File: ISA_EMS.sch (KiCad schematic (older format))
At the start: 91 parts, among them J1 ISA BUS, J10 Parallel Port, J11 Serial 4 IDC, J12 Serial 3 IDC, J13 UART4_SEL, J14 ROM Config, J2 ADDR_IRQ, J3 UART1_SEL, J4 UART2_SEL, J5 ADDR, J6 Serial 2 IDC, J7 Serial 1 DB9, J8 UART3_SEL, J9 Parport IRQ Select, U1 74LS138, U11 74LS30, U12 74LS86, U13 74LS02, U14 74LS155, U15 74LS245, U16 74LS174, U17 74LS374, U18 74LS05, U19 74LS125, U2 74LS138, U20 74LS240, U21 74LS244, U23 16C554, U24 74LS32, U25 GD75232N, U26 GD75232N, U27 SST39SF040, U28 74HCT688, U5 GD75232N, U6 GD75232N, X1 1.8432Mhz

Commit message: Add first ram CHIP
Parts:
- removed C27, C28, C29, C30, C31, C32, C33, C34, C35: 2.2nF, Capacitor_THT:C_Disc_D5.0mm_W2.5mm_P5.00mm, symbol Device:C_Small
- removed D1: LED Channel A, LED_THT:LED_D3.0mm-3, symbol Device:LED_Dual_CAC
- removed D2: LED Channel B, LED_THT:LED_D3.0mm-3, symbol Device:LED_Dual_CAC
- removed D3: LED Channel C, LED_THT:LED_D3.0mm-3, symbol Device:LED_Dual_CAC
- removed D4: LED Channel D, LED_THT:LED_D3.0mm-3, symbol Device:LED_Dual_CAC
- removed J10: Parallel Port, Connector_PinHeader_2.54mm:PinHeader_2x13_P2.54mm_Vertical, symbol Connector_Generic:Conn_02x13_Odd_Even
- removed J11: Serial 4 IDC, Connector_PinHeader_2.54mm:PinHeader_2x05_P2.54mm_Vertical, symbol Connector_Generic:Conn_02x05_Odd_Even
- removed J12: Serial 3 IDC, Connector_PinHeader_2.54mm:PinHeader_2x05_P2.54mm_Vertical, symbol Connector_Generic:Conn_02x05_Odd_Even
- removed J13: UART4_SEL, Connector_PinHeader_2.54mm:PinHeader_1x04_P2.54mm_Vertical, symbol Connector_Generic:Conn_01x04
- removed J2: ADDR_IRQ, Connector_PinHeader_2.54mm:PinHeader_1x08_P2.54mm_Vertical, symbol Connector_Generic:Conn_01x08
- removed J3: UART1_SEL, Connector_PinHeader_2.54mm:PinHeader_1x08_P2.54mm_Vertical, symbol Connector_Generic:Conn_01x08
- removed J4: UART2_SEL, Connector_PinHeader_2.54mm:PinHeader_1x08_P2.54mm_Vertical, symbol Connector_Generic:Conn_01x08
- removed J5: ADDR, Connector_PinHeader_2.54mm:PinHeader_1x04_P2.54mm_Vertical, symbol Connector_Generic:Conn_01x04
- removed J6: Serial 2 IDC, Connector_PinHeader_2.54mm:PinHeader_2x05_P2.54mm_Vertical, symbol Connector_Generic:Conn_02x05_Odd_Even
- removed J7: Serial 1 DB9, Connector_Dsub:DSUB-9_Male_Horizontal_P2.77x2.84mm_EdgePinOffset7.70mm_Housed_MountingHolesOffset9.12mm, symbol Connector:DB9_Male_MountingHoles
- removed J8: UART3_SEL, Connector_PinHeader_2.54mm:PinHeader_1x04_P2.54mm_Vertical, symbol Connector_Generic:Conn_01x04
- removed J9: Parport IRQ Select, Connector_PinHeader_2.54mm:PinHeader_2x04_P2.54mm_Vertical, symbol Connector_Generic:Conn_02x04_Odd_Even
- removed JP1: Address selection, Connector_PinHeader_2.54mm:PinHeader_1x02_P2.54mm_Vertical, symbol Device:Jumper_NO_Small
- removed JP2: Parport type, Connector_PinHeader_2.54mm:PinHeader_1x03_P2.54mm_Vertical, symbol Device:Jumper_NC_Dual
- removed JP3: Interrupt Mode, Connector_PinHeader_2.54mm:PinHeader_1x02_P2.54mm_Vertical, symbol Device:Jumper_NO_Small
- removed R10, R3, R4, R5, R6, R7, R8, R9: 1k, Resistor_THT:R_Axial_DIN0207_L6.3mm_D2.5mm_P10.16mm_Horizontal, symbol Device:R_Small
- removed RN1: 4.7k, Resistor_THT:R_Array_SIP9, symbol Device:R_Network08
- removed RN2: 4.7k, Resistor_THT:R_Array_SIP5, symbol Device:R_Network04
- removed U1, U2: 74LS138, Package_DIP:DIP-16_W7.62mm_LongPads, symbol 74xx:74LS138
- removed U11: 74LS30, Package_DIP:DIP-14_W7.62mm_LongPads, symbol 74xx:74LS30
- removed U12: 74LS86, Package_DIP:DIP-14_W7.62mm_LongPads, symbol 74xx:74LS86
- removed U13: 74LS02, Package_DIP:DIP-14_W7.62mm_LongPads, symbol 74xx:74LS02
- removed U14: 74LS155, Package_DIP:DIP-16_W7.62mm_LongPads, symbol 74xx:74LS155
- removed U15: 74LS245, Package_DIP:DIP-20_W7.62mm_LongPads, symbol 74xx:74LS245
- removed U16: 74LS174, Package_DIP:DIP-16_W7.62mm_LongPads, symbol 74xx:74LS174
- removed U17: 74LS374, Package_DIP:DIP-20_W7.62mm_LongPads, symbol 74xx:74LS374
- removed U18: 74LS05, Package_DIP:DIP-14_W7.62mm_LongPads, symbol 74xx:74LS05
- removed U19: 74LS125, Package_DIP:DIP-14_W7.62mm_LongPads, symbol 74xx:74LS125
- removed U20: 74LS240, Package_DIP:DIP-20_W7.62mm_LongPads, symbol 74xx:74LS240
- removed U21: 74LS244, Package_DIP:DIP-20_W7.62mm_LongPads, symbol 74xx:74LS244
- removed U23: 16C554, Package_LCC:PLCC-68_THT-Socket, symbol custom_components:16554
- removed U24: 74LS32, Package_DIP:DIP-14_W7.62mm_LongPads, symbol 74xx:74LS32
- removed U25, U26, U5, U6: GD75232N, Package_DIP:DIP-20_W7.62mm_LongPads, symbol Interface_UART:GD75232N
- removed X1: 1.8432Mhz, ISA_DualUART:Oscillator_DIP-14-8, symbol Oscillator:CXO_DIP14
- added U3: AS6C4008-55PCN, Package_DIP:DIP-32_W15.24mm, symbol Memory_RAM:AS6C4008-55PCN
- renumbered RN3 to RN1, U28 to U1, U27 to U2
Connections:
- net labels added: DB0, DB1, DB2, DB3, DB4, DB5, DB6, DB7, RAM-A14, RAM-A15, RAM-A16, RAM-A17, RAM-A18, ~RAM-CS0
- net labels removed: 0x2E8, 0x2F8, 0x3E8, 0x3F8, PARPORT_BD0, PARPORT_BD1, PARPORT_BD2, PARPORT_BD3, PARPORT_BD4, PARPORT_BD5, PARPORT_BD6, PARPORT_BD7, PARPORT_BUSY, PARPORT_DATA0, PARPORT_DATA1, PARPORT_DATA2, PARPORT_DATA3, PARPORT_DATA4, PARPORT_DATA5, PARPORT_DATA6, PARPORT_DATA7, PARPORT_DIR, PARPORT_IRQ, PARPORT_IRQEN, PARPORT_PE, PARPORT_R, PARPORT_RPA, PARPORT_RPB, PARPORT_RPC, PARPORT_SLCT, PARPORT_WPA, PARPORT_WPC, RN_1, RN_2, RN_3, RN_4, RN_5, RN_6, RN_7, RN_8, RS232_1_CTS, RS232_1_DCD, RS232_1_DSR, RS232_1_DTR, RS232_1_RI, RS232_1_RTS, RS232_1_RX, RS232_1_TX, RS232_2_CTS, RS232_2_DCD, RS232_2_DSR, RS232_2_DTR, RS232_2_RI, RS232_2_RTS, RS232_2_RX, RS232_2_TX, RS232_3_CTS, RS232_3_DCD, RS232_3_DSR, RS232_3_DTR, RS232_3_RI, RS232_3_RTS, RS232_3_RX, RS232_3_TX, RS232_4_CTS, RS232_4_DCD, RS232_4_DSR, RS232_4_DTR, RS232_4_RI, RS232_4_RTS, RS232_4_RX, RS232_4_TX, RX_A, RX_B, RX_C, RX_D, SER_CLK, TX_A, TX_B, TX_C, TX_D, UART1_IRQ, UART2_IRQ, UARTA_IRQ, UARTB_IRQ, UARTC_IRQ, UARTD_IRQ, ~CTS_A, ~CTS_B, ~CTS_C, ~CTS_D, ~DCD_A, ~DCD_B, ~DCD_C, ~DCD_D, ~DSR_A, ~DSR_B, ~DSR_C, ~DSR_D, ~DTR_A, ~DTR_B, ~DTR_C, ~DTR_D, ~PARPORT_ACK, ~PARPORT_AUTOFD, ~PARPORT_ERROR, ~PARPORT_INIT, ~PARPORT_IRQEN, ~PARPORT_RESET, ~PARPORT_SLCTIN, ~PARPORT_STROBE, ~RI_A, ~RI_B, ~RI_C, ~RI_D, ~RTS_A, ~RTS_B, ~RTS_C, ~RTS_D, ~UART1_CS, ~UART2_CS, ~UART3_CS, ~UART4_CS
- wire segments 950 -> 310
- no-connect marks 37 -> 13
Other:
- note removed: "Open - 0x278/9/A\nClosed - 0x378/9/A"
- note removed: "Parallel Port"
- note removed: "Serial Ports"

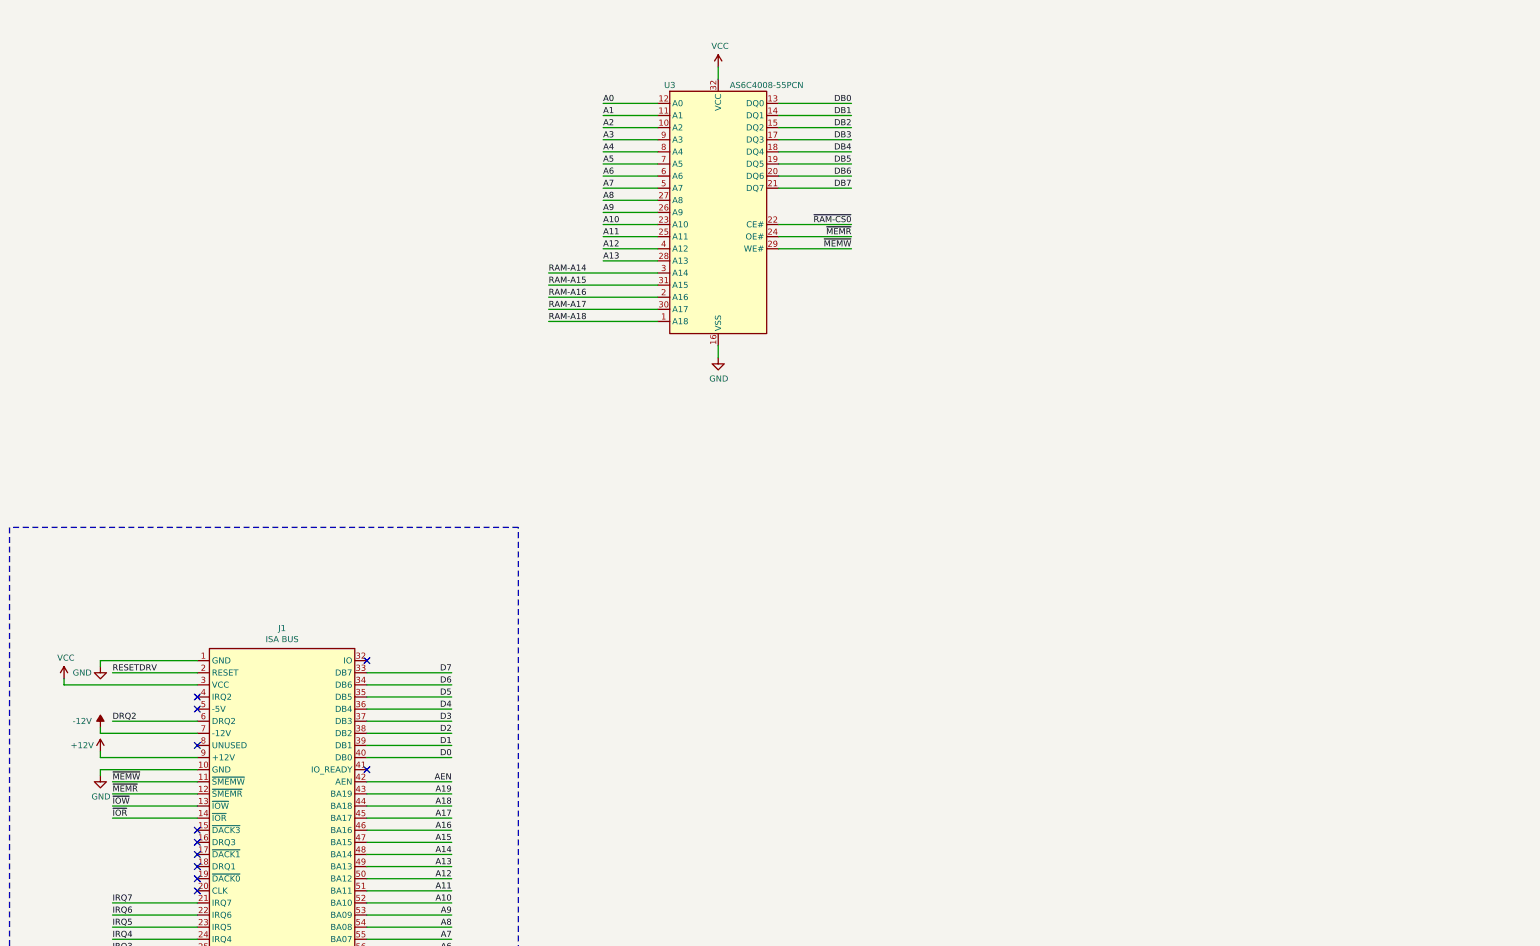
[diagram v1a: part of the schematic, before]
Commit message: Add all the necessary RAM chips
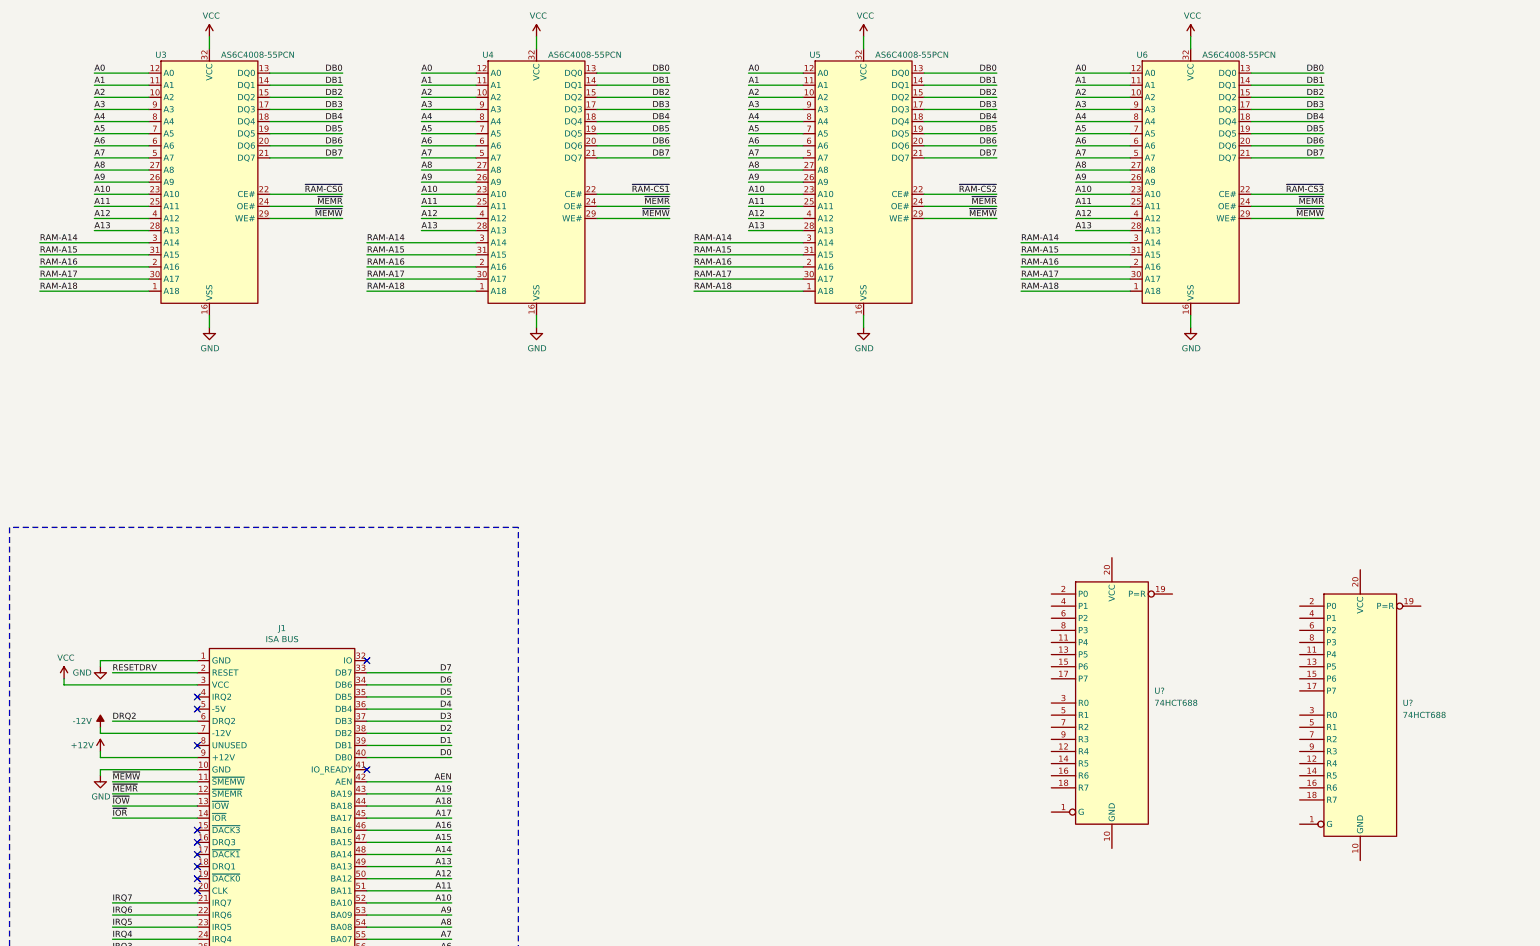
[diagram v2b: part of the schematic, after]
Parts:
- added U4, U5, U6: AS6C4008-55PCN, Package_DIP:DIP-32_W15.24mm, symbol Memory_RAM:AS6C4008-55PCN
- added U? (x2): 74HCT688, Package_DIP:DIP-20_W7.62mm_LongPads, symbol 74xx:74HCT688
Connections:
- net A0: now also U4.12 (A0), U5.12 (A0), U6.12 (A0)
- net A1: now also U4.11 (A1), U5.11 (A1), U6.11 (A1)
- net A10: now also U4.23 (A10), U5.23 (A10), U6.23 (A10)
- net A11: now also U4.25 (A11), U5.25 (A11), U6.25 (A11)
- net A12: now also U4.4 (A12), U5.4 (A12), U6.4 (A12)
- net A13: now also U4.28 (A13), U5.28 (A13), U6.28 (A13)
- net A2: now also U4.10 (A2), U5.10 (A2), U6.10 (A2)
- net A3: now also U4.9 (A3), U5.9 (A3), U6.9 (A3)
- net A4: now also U4.8 (A4), U5.8 (A4), U6.8 (A4)
- net A5: now also U4.7 (A5), U5.7 (A5), U6.7 (A5)
- net A6: now also U4.6 (A6), U5.6 (A6), U6.6 (A6)
- net A7: now also U4.5 (A7), U5.5 (A7), U6.5 (A7)
- net A8: now also U4.27 (A8), U5.27 (A8), U6.27 (A8)
- net A9: now also U4.26 (A9), U5.26 (A9), U6.26 (A9)
- net DB0: now also U4.13 (DQ0), U5.13 (DQ0), U6.13 (DQ0)
- net DB1: now also U4.14 (DQ1), U5.14 (DQ1), U6.14 (DQ1)
- net DB2: now also U4.15 (DQ2), U5.15 (DQ2), U6.15 (DQ2)
- net DB3: now also U4.17 (DQ3), U5.17 (DQ3), U6.17 (DQ3)
- net DB4: now also U4.18 (DQ4), U5.18 (DQ4), U6.18 (DQ4)
- net DB5: now also U4.19 (DQ5), U5.19 (DQ5), U6.19 (DQ5)
- net DB6: now also U4.20 (DQ6), U5.20 (DQ6), U6.20 (DQ6)
- net DB7: now also U4.21 (DQ7), U5.21 (DQ7), U6.21 (DQ7)
- net GND: now also U4.16 (VSS), U5.16 (VSS), U6.16 (VSS)
- net RAM-A14: now also U4.3 (A14), U5.3 (A14), U6.3 (A14)
- net RAM-A15: now also U4.31 (A15), U5.31 (A15), U6.31 (A15)
- net RAM-A16: now also U4.2 (A16), U5.2 (A16), U6.2 (A16)
- net RAM-A17: now also U4.30 (A17), U5.30 (A17), U6.30 (A17)
- net RAM-A18: now also U4.1 (A18), U5.1 (A18), U6.1 (A18)
- net VCC: now also U4.32 (VCC), U5.32 (VCC), U6.32 (VCC)
- net ~MEMR: now also U4.24 (OE#), U5.24 (OE#), U6.24 (OE#)
- net ~MEMW: now also U4.29 (WE#), U5.29 (WE#), U6.29 (WE#)
- new net ~RAM-CS1: U4.22 (CE#)
- new net ~RAM-CS2: U5.22 (CE#)
- new net ~RAM-CS3: U6.22 (CE#)
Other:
- moved on the sheet: U3

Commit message: Import schematics from lo-tech ems board
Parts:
- added C21: 100nF, Capacitor_THT:C_Disc_D6.0mm_W2.5mm_P5.00mm, symbol Device:C_Small
- added J2: EMS Address, Connector_PinHeader_2.54mm:PinHeader_2x04_P2.54mm_Vertical, symbol Connector_Generic:Conn_02x04_Odd_Even
- added RN2: 10k, Resistor_THT:R_Array_SIP5, symbol Device:R_Network04
- added RN3: 10k, Resistor_THT:R_Array_SIP9, symbol Device:R_Network08
- added U10: 74HCT32, Package_DIP:DIP-14_W7.62mm_LongPads, symbol 74xx:74LS32
- added U11: 74HCT04, Package_DIP:DIP-14_W7.62mm_LongPads, symbol 74xx:74HCT04
- added U12: 74ACT245, Package_DIP:DIP-20_W7.62mm_LongPads, symbol 74xx:74LS245
- added U13, U14, U15, U16: AS6C4008-55PCN, Package_DIP:DIP-32_W15.24mm, symbol Memory_RAM:AS6C4008-55PCN
- added U17: 74HCT138, Package_DIP:DIP-16_W7.62mm_LongPads, symbol 74xx:74LS138
- added U18, U19, U20, U21: 74LS573, Package_DIP:DIP-20_W7.62mm_LongPads, symbol 74xx:74LS573
- added U9: 74HCT139, Package_DIP:DIP-16_W7.62mm_LongPads, symbol 74xx:74LS139
- gave numbers to parts that had none: 2
- renumbered J14 to J1
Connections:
- net A0: now also U13.12 (A0), U14.12 (A0), U15.12 (A0), U16.12 (A0), U9.2 (A0)
- net A1: now also U13.11 (A1), U14.11 (A1), U15.11 (A1), U16.11 (A1), U9.3 (A1)
- net A10: now also U13.23 (A10), U14.23 (A10), U15.23 (A10), U16.23 (A10)
- net A11: now also U13.25 (A11), U14.25 (A11), U15.25 (A11), U16.25 (A11)
- net A12: now also U13.4 (A12), U14.4 (A12), U15.4 (A12), U16.4 (A12)
- net A13: now also U13.28 (A13), U14.28 (A13), U15.28 (A13), U16.28 (A13)
- net A14: now also U9.14 (A0)
- net A15: now also U9.13 (A1)
- net A16: now also U7.11 (P4)
- net A17: now also U7.13 (P5)
- net A18: now also U7.15 (P6)
- net A19: now also U7.17 (P7)
- net A2: now also U8.2 (P0), U13.10 (A2), U14.10 (A2), U15.10 (A2), U16.10 (A2)
- net A3: now also U8.4 (P1), U13.9 (A3), U14.9 (A3), U15.9 (A3), U16.9 (A3)
- net A4: now also U8.6 (P2), U13.8 (A4), U14.8 (A4), U15.8 (A4), U16.8 (A4)
- net A5: now also U8.8 (P3), U13.7 (A5), U14.7 (A5), U15.7 (A5), U16.7 (A5)
- net A6: now also U8.17 (P7), U13.6 (A6), U14.6 (A6), U15.6 (A6), U16.6 (A6)
- net A7: now also U8.15 (P6), U13.5 (A7), U14.5 (A7), U15.5 (A7), U16.5 (A7)
- net A8: now also U8.13 (P5), U13.27 (A8), U14.27 (A8), U15.27 (A8), U16.27 (A8)
- net A9: now also U8.11 (P4), U13.26 (A9), U14.26 (A9), U15.26 (A9), U16.26 (A9)
- net AEN: now also U8.1 (G)
- net D0: now also U12.2 (A0), U18.2 (D0), U19.2 (D0), U20.2 (D0), U21.2 (D0)
- net D1: now also U12.3 (A1), U18.3 (D1), U19.3 (D1), U20.3 (D1), U21.3 (D1)
- net D2: now also U12.4 (A2), U18.4 (D2), U19.4 (D2), U20.4 (D2), U21.4 (D2)
- net D3: now also U12.5 (A3), U18.5 (D3), U19.5 (D3), U20.5 (D3), U21.5 (D3)
- net D4: now also U12.6 (A4), U18.6 (D4), U19.6 (D4), U20.6 (D4), U21.6 (D4)
- net D5: now also U12.7 (A5), U18.7 (D5), U19.7 (D5), U20.7 (D5), U21.7 (D5)
- net D6: now also U12.8 (A6), U18.8 (D6), U19.8 (D6), U20.8 (D6), U21.8 (D6)
- net D7: now also U12.9 (A7), U18.9 (D7), U19.9 (D7), U20.9 (D7), U21.9 (D7)
- net DB0: now also RN3.2 (R1), U12.18 (B0), U13.13 (DQ0), U14.13 (DQ0), U15.13 (DQ0), U16.13 (DQ0)
- net DB1: now also RN3.3 (R2), U12.17 (B1), U13.14 (DQ1), U14.14 (DQ1), U15.14 (DQ1), U16.14 (DQ1)
- net DB2: now also RN3.4 (R3), U12.16 (B2), U13.15 (DQ2), U14.15 (DQ2), U15.15 (DQ2), U16.15 (DQ2)
- net DB3: now also RN3.5 (R4), U12.15 (B3), U13.17 (DQ3), U14.17 (DQ3), U15.17 (DQ3), U16.17 (DQ3)
- net DB4: now also RN3.6 (R5), U12.14 (B4), U13.18 (DQ4), U14.18 (DQ4), U15.18 (DQ4), U16.18 (DQ4)
- net DB5: now also RN3.7 (R6), U12.13 (B5), U13.19 (DQ5), U14.19 (DQ5), U15.19 (DQ5), U16.19 (DQ5)
- net DB6: now also RN3.8 (R7), U12.12 (B6), U13.20 (DQ6), U14.20 (DQ6), U15.20 (DQ6), U16.20 (DQ6)
- net DB7: now also RN3.9 (R8), U12.11 (B7), U13.21 (DQ7), U14.21 (DQ7), U15.21 (DQ7), U16.21 (DQ7)
- net GND: now also U7.1 (G), U7.10 (GND), U7.2 (P0), U7.3 (R0), U7.4 (P1), U7.5 (R1), U7.6 (P2), U7.7 (R2), U7.8 (P3), U7.9 (R3), U8.10 (GND), U8.14 (R5), U8.16 (R6), U8.7 (R2), C21.2, J2.1 (Pin_1), J2.3 (Pin_3), J2.5 (Pin_5), J2.7 (Pin_7), U10.10, U10.4, U10.5, U10.7 (GND), U10.9, U11.11, U11.12, U11.13, U11.13, U11.7 (GND), U12.10 (GND), U13.16 (VSS), U14.16 (VSS), U15.16 (VSS), U16.16 (VSS), U17.4 (E1), U17.8 (GND), U18.10 (GND), U19.10 (GND), U20.10 (GND), U21.10 (GND), U9.8 (GND)
- net RAM-A14: now also U13.3 (A14), U14.3 (A14), U15.3 (A14), U16.3 (A14), U18.19 (Q0), U19.19 (Q0), U20.19 (Q0), U21.19 (Q0)
- net RAM-A15: now also U13.31 (A15), U14.31 (A15), U15.31 (A15), U16.31 (A15), U18.18 (Q1), U19.18 (Q1), U20.18 (Q1), U21.18 (Q1)
- net RAM-A16: now also U13.2 (A16), U14.2 (A16), U15.2 (A16), U16.2 (A16), U18.17 (Q2), U19.17 (Q2), U20.17 (Q2), U21.17 (Q2)
- net RAM-A17: now also U13.30 (A17), U14.30 (A17), U15.30 (A17), U16.30 (A17), U18.16 (Q3), U19.16 (Q3), U20.16 (Q3), U21.16 (Q3)
- net RAM-A18: now also U13.1 (A18), U14.1 (A18), U15.1 (A18), U16.1 (A18), U18.15 (Q4), U19.15 (Q4), U20.15 (Q4), U21.15 (Q4)
- net VCC: now also U7.16 (R6), U7.18 (R7), U7.20 (VCC), U8.12 (R4), U8.18 (R7), U8.20 (VCC), U8.9 (R3), C21.1, RN2.1 (common), RN3.1 (common), U10.14 (VCC), U11.14 (VCC), U12.20 (VCC), U13.32 (VCC), U14.32 (VCC), U15.32 (VCC), U16.32 (VCC), U17.16 (VCC), U17.6 (E3), U18.20 (VCC), U19.20 (VCC), U20.20 (VCC), U21.20 (VCC), U9.16 (VCC)
- net ~IOW: now also U10.2
- net ~MEMR: now also U12.1 (A->B), U13.24 (OE#), U14.24 (OE#), U15.24 (OE#), U16.24 (OE#)
- net ~MEMW: now also U13.29 (WE#), U14.29 (WE#), U15.29 (WE#), U16.29 (WE#)
- net ~RAM-CS0: now also U17.15 (O0)
- net ~RAM-CS1: now also U17.14 (O1)
- net ~RAM-CS2: now also U17.13 (O2)
- net ~RAM-CS3: now also U17.12 (O3)
- net JP1: now reaches U7.12 (R4)
- net JP1: now also J2.2 (Pin_2), RN2.2 (R1)
- net JP2: now reaches U7.14 (R5)
- net JP2: now also J2.4 (Pin_4), RN2.3 (R2)
- net ~RAM-SELECT: now reaches U7.19 (P=R)
- net ~RAM-SELECT: now also U12.19 (CE), U17.5 (E2), U9.15 (E)
- net at U8.19 (P=R): now also U10.1
- net JP3: now reaches U8.3 (R0)
- net JP3: now also J2.6 (Pin_6), RN2.4 (R3)
- net JP4: now reaches U8.5 (R1)
- net JP4: now also J2.8 (Pin_8), RN2.5 (R4)
- new net: U10.3, U9.1 (E)
- new net: U11.1, U9.4 (O0)
- new net: U11.3, U9.5 (O1)
- new net: U11.5, U9.6 (O2)
- new net: U11.9, U9.7 (O3)
- new net RAM-A19: U17.1 (A0), U18.14 (Q5), U19.14 (Q5), U20.14 (Q5), U21.14 (Q5)
- new net RAM-A20: U17.2 (A1), U18.13 (Q6), U19.13 (Q6), U20.13 (Q6), U21.13 (Q6)
- new net RAM-A21: U17.3 (A2), U18.12 (Q7), U19.12 (Q7), U20.12 (Q7), U21.12 (Q7)
- new net REG0-LOAD: U11.2, U18.11 (Load)
- new net REG1-LOAD: U11.4, U19.11 (Load)
- new net REG2-LOAD: U11.6, U20.11 (Load)
- new net REG3-LOAD: U11.8, U21.11 (Load)
- new net ~RAM-CS4: U13.22 (CE#), U17.11 (O4)
- new net ~RAM-CS5: U14.22 (CE#), U17.10 (O5)
- new net ~RAM-CS6: U15.22 (CE#), U17.9 (O6)
- new net ~RAM-CS7: U16.22 (CE#), U17.7 (O7)
- new net ~REG0-OE: U18.1 (OE), U9.12 (O0)
- new net ~REG1-OE: U19.1 (OE), U9.11 (O1)
- new net ~REG2-OE: U20.1 (OE), U9.10 (O2)
- new net ~REG3-OE: U21.1 (OE), U9.9 (O3)
- no-connect marks 13 -> 18
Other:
- moved on the sheet: U7, U8

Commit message: Update schematic, draw board
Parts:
- added D1: EMS in use, LED_THT:LED_D3.0mm_Clear, symbol Device:LED_Small
- added H1, H2: MountingHole_Pad, symbol Mechanical:MountingHole_Pad
- added R3: 1k, Resistor_THT:R_Axial_DIN0207_L6.3mm_D2.5mm_P10.16mm_Horizontal, symbol Device:R_Small
- U10: renamed from U11; value 74HCT04 -> 74HCT32
- renumbered J1 to J3
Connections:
- net GND: now also H1.1, H2.1
- net VCC: now also D1.2 (A)
- net ~RAM-SELECT: now also R3.1
- new net: D1.1 (K), R3.2
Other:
- note added: "Schematics taken from https://www.lo-tech.co.uk/wiki/Lo-tech_2MB_EMS_Board with small modifications."
